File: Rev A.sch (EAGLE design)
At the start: 7 parts

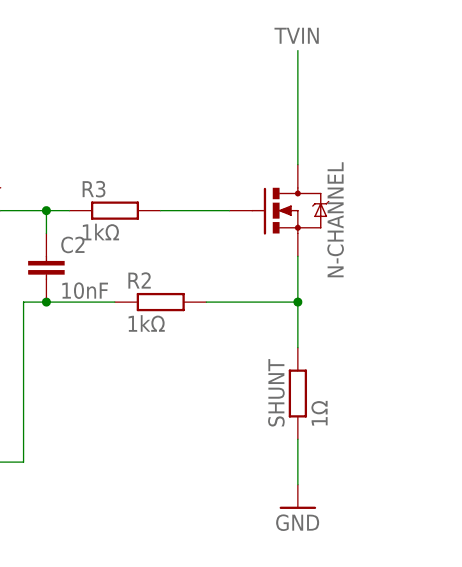
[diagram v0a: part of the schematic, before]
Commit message: Added the heatsink
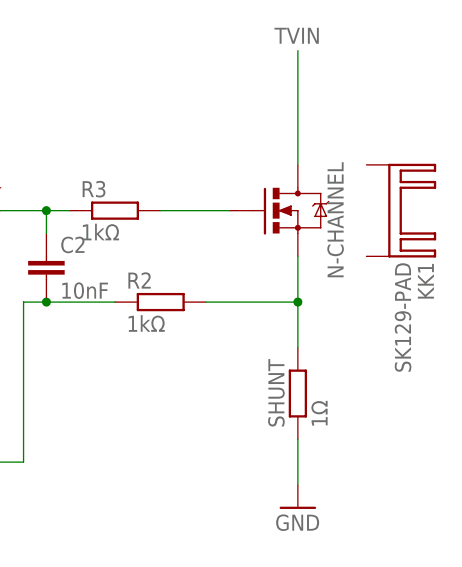
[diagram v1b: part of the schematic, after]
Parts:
- added KK1: SK129-PAD, heatsink:SK129-PAD
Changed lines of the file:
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@@
 <part name="R3" library="rcl" deviceset="R-EU_" device="R0805" value="1kΩ"/>
 <part name="C2" library="rcl" deviceset="C-EU" device="C0805" value="10nF"/>
+<part name="KK1" library="heatsink" deviceset="SK129-PAD" device=""/>
 </parts>
 <sheets>
@@
 <instance part="R3" gate="G$1" x="111.76" y="55.88"/>
 <instance part="C2" gate="G$1" x="104.14" y="50.8"/>
+<instance part="KK1" gate="G$1" x="142.24" y="55.88" rot="R270"/>
 </instances>
 <busses>

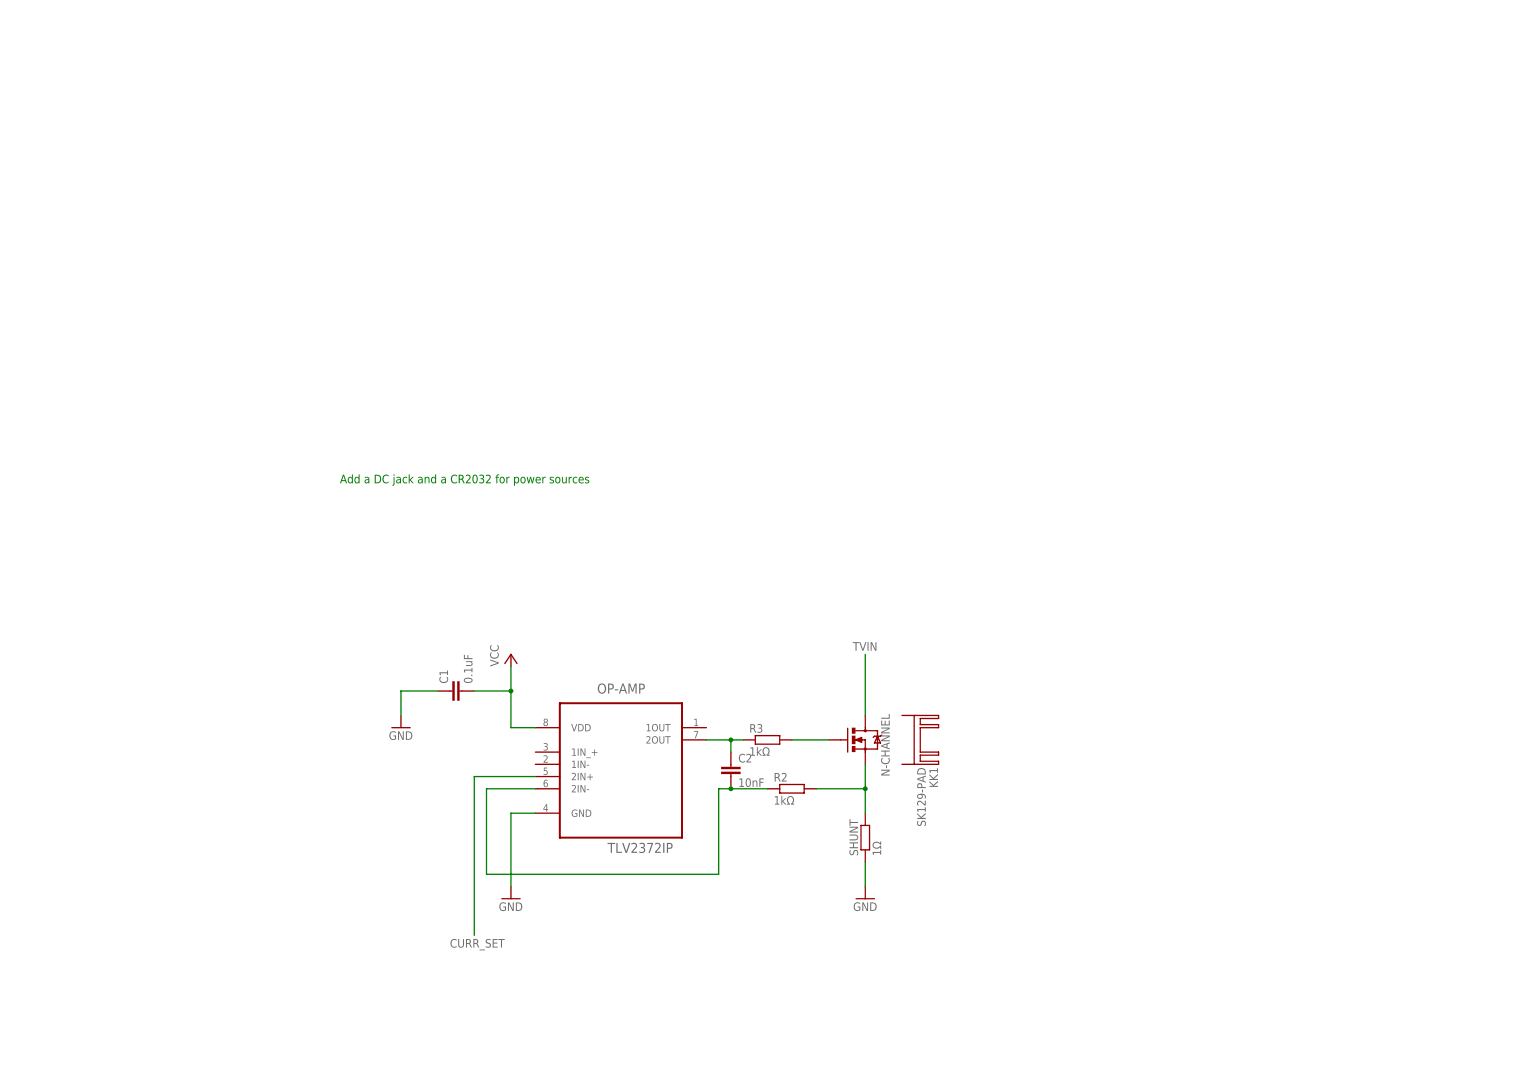
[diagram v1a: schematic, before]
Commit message: Added the power input
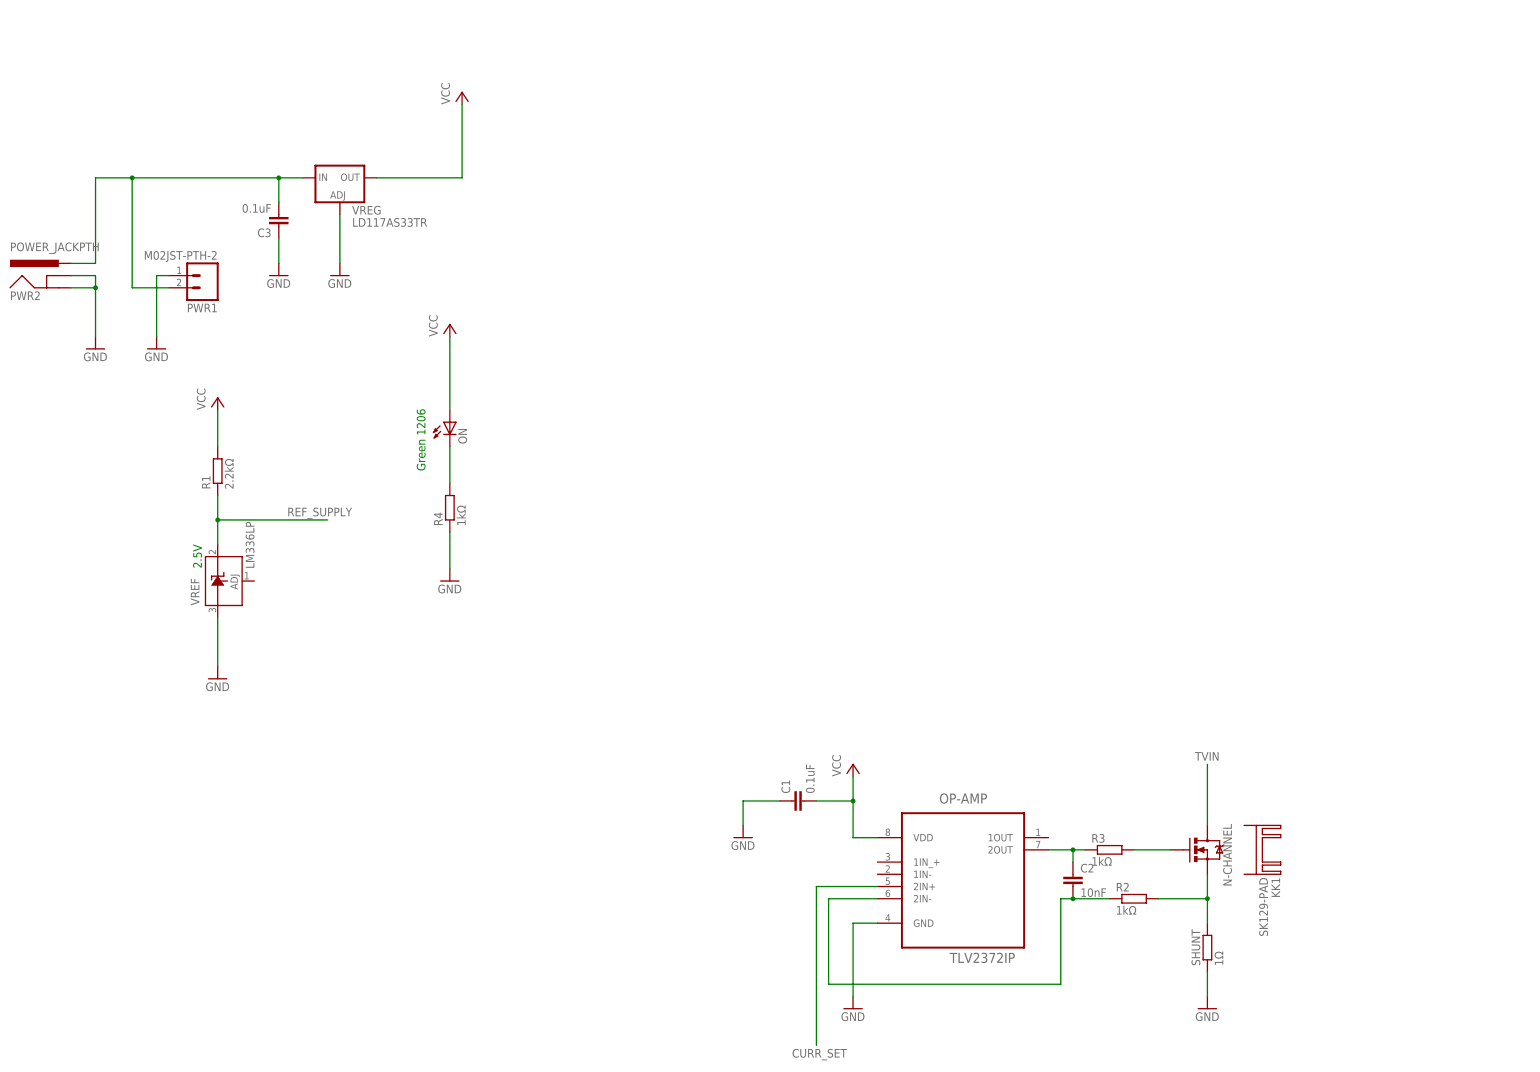
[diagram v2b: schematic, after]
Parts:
- added C3: 0.1uF, rcl:C-EUC0805
- added ON: (no value), led:LEDCHIPLED_1206
- added PWR1: M02JST-PTH-2, SparkFun-Connectors:M02JST-PTH-2
- added PWR2: POWER_JACKPTH, SparkFun-Connectors:POWER_JACKPTH
- added R1: 2.2kΩ, rcl:R-EU_R0805
- added R4: 1kΩ, rcl:R-EU_R0805
- added VREF: LM336LP, linear:LM336LP
- added VREG: LD117AS33TR, v-reg:LD117AS33TR
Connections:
- new net N$6: C3.2, PWR1.2, PWR2.PWR, VREG.IN
- new net N$7: ON.C, R4.2
- new net REF_SUPPLY: R1.1, VREF.C
- net GND: now also C3.1, PWR1.1, PWR2.GND, PWR2.GNDBREAK, R4.1, VREF.A, VREG.ADJ
- net VCC: now also ON.A, R1.2, VREG.OUT
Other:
- note added: "2.5V"
- note added: "Green 1206"
- note removed: "Add a DC jack and a CR2032 for power sources"
- moved on the sheet: C1, C2, KK1, N-CHANNEL, OP-AMP, R2, R3, SHUNT

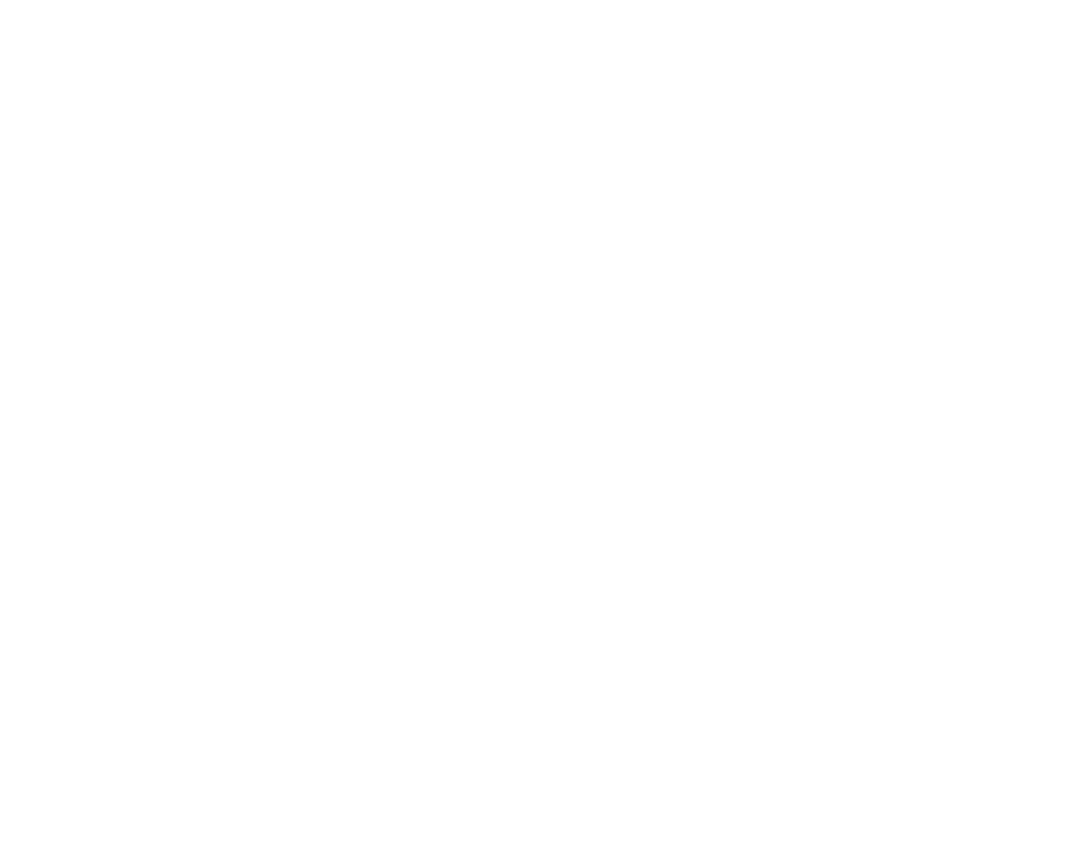
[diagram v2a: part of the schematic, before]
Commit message: Added the MCU
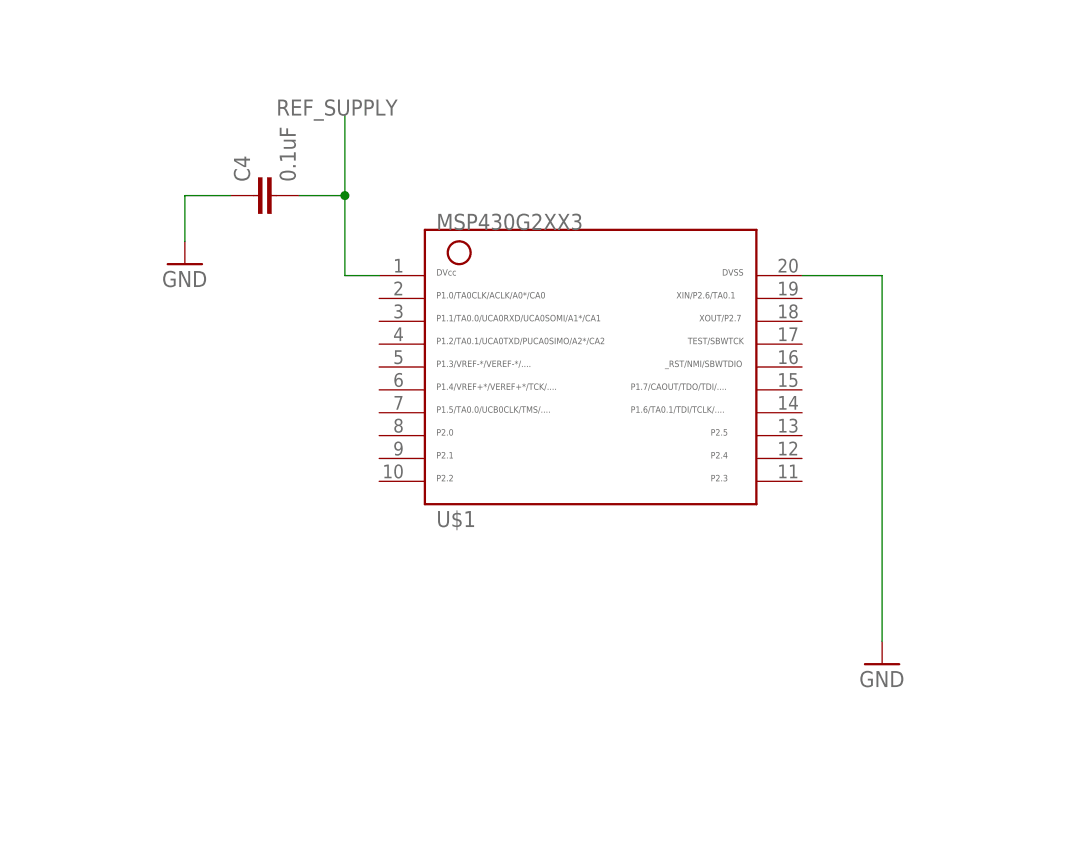
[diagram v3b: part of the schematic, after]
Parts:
- added C4: 0.1uF, rcl:C-EUC0805
- added U$1: G2XX3---N20, TI_MSP430_v16:G2XX3---N20
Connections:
- net GND: now also C4.1, U$1.20
- net REF_SUPPLY: now also C4.2, U$1.1
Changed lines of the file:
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@@
 <setting verticaltext="up"/>
 </settings>
-<grid distance="0.1" unitdist="inch" unit="inch" style="lines" multiple="1" display="no" altdistance="0.01" altunitdist="inch" altunit="inch"/>
+<grid distance="0.05" unitdist="inch" unit="inch" style="lines" multiple="1" display="no" altdistance="0.01" altunitdist="inch" altunit="inch"/>
 <layers>
 <layer number="1" name="Top" color="4" fill="1" visible="no" active="no"/>
@@
 <part name="R4" library="rcl" deviceset="R-EU_" device="R0805" value="1kΩ"/>
 <part name="GND9" library="supply1" deviceset="GND" device=""/>
+<part name="U$1" library="TI_MSP430_v16" deviceset="G2XX3---N20" device=""/>
+<part name="GND10" library="supply1" deviceset="GND" device=""/>
+<part name="GND11" library="supply1" deviceset="GND" device=""/>
+<part name="C4" library="rcl" deviceset="C-EU" device="C0805" value="0.1uF"/>
 </parts>
 <sheets>
@@
 <instance part="R4" gate="G$1" x="45.72" y="104.14" rot="R90"/>
 <instance part="GND9" gate="1" x="45.72" y="88.9"/>
+<instance part="U$1" gate="G$1" x="157.48" y="157.48"/>
+<instance part="GND10" gate="1" x="189.23" y="121.92"/>
+<instance part="GND11" gate="1" x="111.76" y="166.37"/>
+<instance part="C4" gate="G$1" x="119.38" y="173.99" rot="R90"/>
 </instances>
 <busses>
@@
 <wire x1="45.72" y1="99.06" x2="45.72" y2="91.44" width="0.1524" layer="91"/>
 <pinref part="GND9" gate="1" pin="GND"/>
+</segment>
+<segment>
+<pinref part="U$1" gate="G$1" pin="20"/>
+<wire x1="180.34" y1="165.1" x2="189.23" y2="165.1" width="0.1524" layer="91"/>
+<wire x1="189.23" y1="165.1" x2="189.23" y2="124.46" width="0.1524" layer="91"/>
+<pinref part="GND10" gate="1" pin="GND"/>
+</segment>
+<segment>
+<pinref part="C4" gate="G$1" pin="1"/>
+<pinref part="GND11" gate="1" pin="GND"/>
+<wire x1="116.84" y1="173.99" x2="111.76" y2="173.99" width="0.1524" layer="91"/>
+<wire x1="111.76" y1="173.99" x2="111.76" y2="168.91" width="0.1524" layer="91"/>
 </segment>
 </net>
@@
 <label x="25.4" y="104.14" size="1.778" layer="95" rot="R180"/>
 </segment>
+<segment>
+<pinref part="U$1" gate="G$1" pin="1"/>
+<wire x1="133.35" y1="165.1" x2="129.54" y2="165.1" width="0.1524" layer="91"/>
+<wire x1="129.54" y1="165.1" x2="129.54" y2="173.99" width="0.1524" layer="91"/>
+<label x="121.92" y="182.88" size="1.778" layer="95"/>
+<junction x="129.54" y="173.99"/>
+<wire x1="129.54" y1="173.99" x2="129.54" y2="182.88" width="0.1524" layer="91"/>
+<pinref part="C4" gate="G$1" pin="2"/>
+<wire x1="124.46" y1="173.99" x2="129.54" y2="173.99" width="0.1524" layer="91"/>
+</segment>
 </net>
 <net name="N$7" class="0">
@@
 </sheet>
 </sheets>
+<errors>
+</errors>
 </schematic>
 </drawing>
